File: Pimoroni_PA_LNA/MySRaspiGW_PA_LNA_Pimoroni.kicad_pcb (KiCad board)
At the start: 2 copper layers, 11.8 x 15.5 mm, 5 parts, among them P1 CONN_02X04, U1 NRF24L01

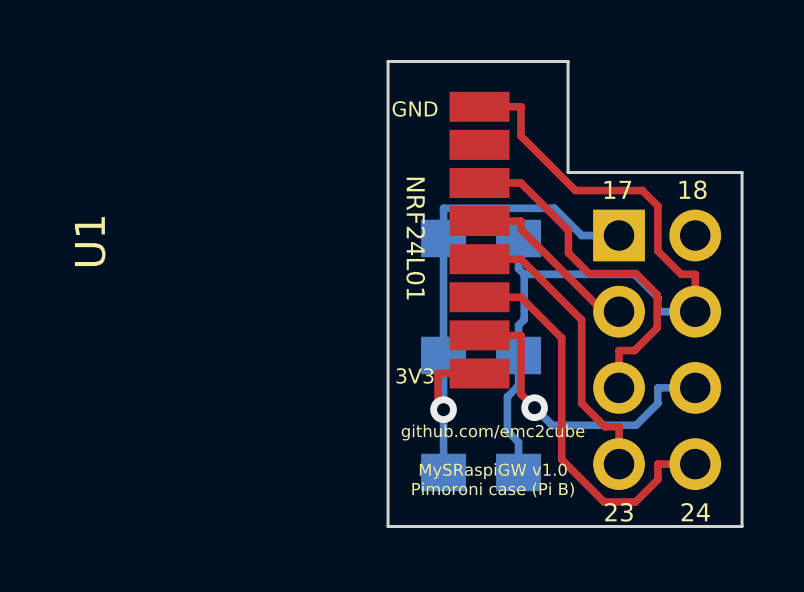
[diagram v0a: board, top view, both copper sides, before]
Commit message: v1.1 IRQ support
Added IRQ support on pin 18
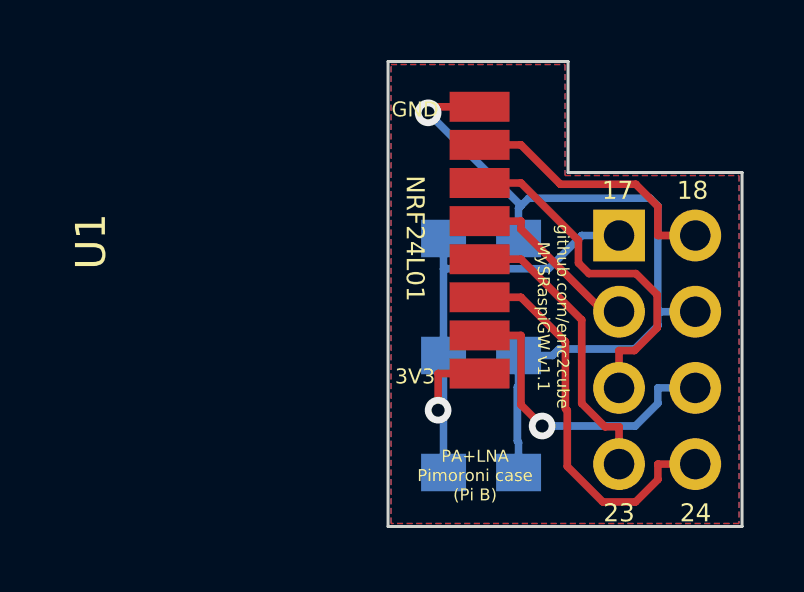
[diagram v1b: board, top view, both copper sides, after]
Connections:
- P1 pad 2: Net-(P1-Pad2) -> IRQ
- U1 pad 8: Net-(U1-Pad8) -> IRQ
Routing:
- net IRQ: track 0.00 -> 9.01 mm
- net +3V3: track 17.7 -> 16.9 mm
- net GND: track 27.0 -> 26.3 mm, vias 0 -> 1
- added copper zone on B.Cu, net GND
- added copper zone on F.Cu, net GND
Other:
- board text added: "PA+LNA Pimoroni case (Pi B)"
- board text added: "github.com/emc2cube MySRaspiGW v1.1"
- board text removed: "github.com/emc2cube MySRaspiGW v1.0 Pimoroni case (Pi B)"
